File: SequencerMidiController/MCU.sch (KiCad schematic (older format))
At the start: 8 parts, among them J6 Conn_02x02_Counter_Clockwise, U33 STM32G0B1_KxTxN_LQFP32

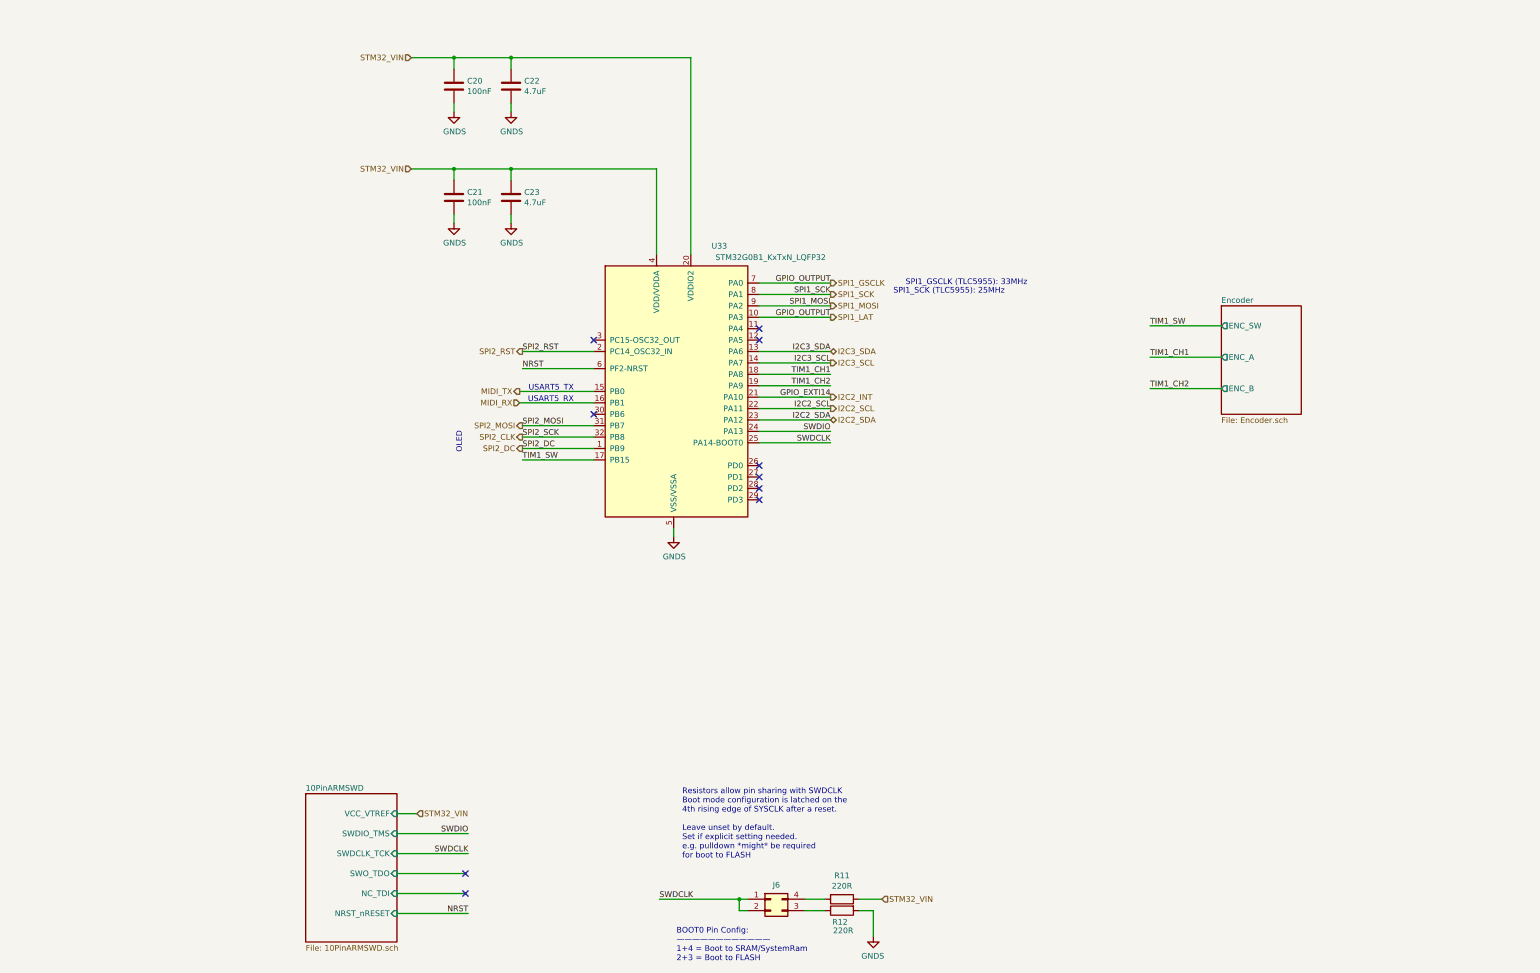
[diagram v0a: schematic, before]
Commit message: RevA Layout draft completed
- Needs tidy up
- Add test points
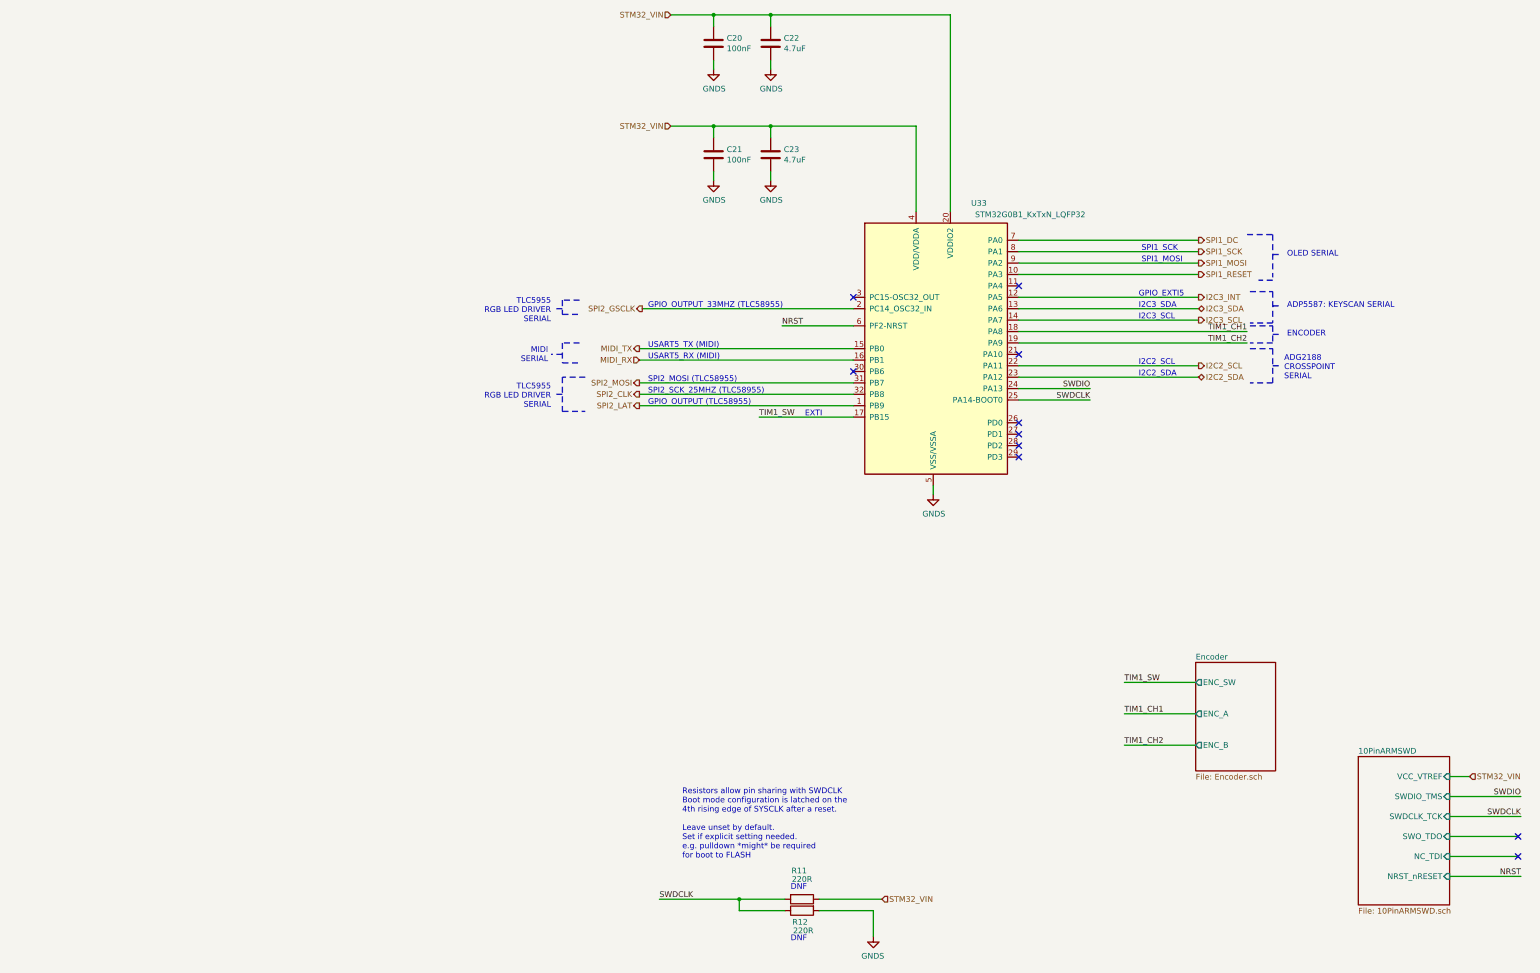
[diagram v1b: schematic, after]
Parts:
- removed J6: Conn_02x02_Counter_Clockwise, Connector_PinHeader_2.54mm:PinHeader_2x02_P2.54mm_Vertical, symbol Connector_Generic:Conn_02x02_Counter_Clockwise
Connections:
- net SWDCLK: now also R11.2, R12.1
- net I2C3_INT: now reaches U33.12 (PA5)
- net I2C2_INT: no longer names the net of U33.21 (PA10)
- net SPI1_GSCLK renamed SPI1_DC
- net SPI1_DC: no longer U33.10 (PA3)
- net SPI2_DC renamed SPI2_LAT
- net SPI2_RST renamed SPI2_GSCLK
- new net SPI1_RESET: U33.10 (PA3)
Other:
- note added: "ADG2188\nCROSSPOINT\nSERIAL"
- note added: "ADP5587: KEYSCAN SERIAL"
- note added: "DNF"
- note added: "ENCODER"
- note added: "EXTI"
- note added: "GPIO_EXTI5"
- note added: "GPIO_OUTPUT (TLC58955)"
- note added: "GPIO_OUTPUT_33MHZ (TLC58955)"
- note added: "I2C2_SCL"
- note added: "I2C2_SDA"
- note added: "I2C3_SCL"
- note added: "I2C3_SDA"
- note added: "MIDI\nSERIAL"
- note added: "OLED SERIAL"
- note added: "SPI1_MOSI"
- note added: "SPI1_SCK"
- note added: "SPI2_MOSI (TLC58955)"
- note added: "SPI2_SCK_25MHZ (TLC58955)"
- note added: "TLC5955\nRGB LED DRIVER\nSERIAL"
- note added: "USART5_RX (MIDI)"
- note added: "USART5_TX (MIDI)"
- note removed: "BOOT0 Pin Config:\n————————————\n1+4 = Boot to SRAM/SystemRam\n2+3 = Boot to FLASH"
- note removed: "OLED"
- note removed: "SPI1_GSCLK (TLC5955): 33MHz"
- note removed: "SPI1_SCK (TLC5955): 25MHz"
- note removed: "USART5_RX"
- note removed: "USART5_TX"
- moved on the sheet: C20, C21, C22, C23, R11, R12, U33

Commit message: Completed RevA layout
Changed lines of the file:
@@
 	10475 5700 10475 5625
 $Sheet
-S 14200 8000 800  1300
+S 4950 6425 800  1300
 U 63BA09FD
 F0 "10PinARMSWD" 50
 F1 "10PinARMSWD.sch" 50
-F2 "VCC_VTREF" I R 15000 8175 50
-F3 "SWDIO_TMS" I R 15000 8350 50
-F4 "SWDCLK_TCK" I R 15000 8525 50
-F5 "SWO_TDO" I R 15000 8700 50
-F6 "NC_TDI" I R 15000 8875 50
-F7 "NRST_nRESET" I R 15000 9050 50
+F2 "VCC_VTREF" I R 5750 6600 50
+F3 "SWDIO_TMS" I R 5750 6775 50
+F4 "SWDCLK_TCK" I R 5750 6950 50
+F5 "SWO_TDO" I R 5750 7125 50
+F6 "NC_TDI" I R 5750 7300 50
+F7 "NRST_nRESET" I R 5750 7475 50
 $EndSheet
 Wire Wire Line
-	15000 8175 15175 8175
-Text HLabel 15175 8175 2    50   Input ~ 0
+	5750 6600 5925 6600
+Text HLabel 5925 6600 2    50   Input ~ 0
 STM32_VIN
 Wire Wire Line
-	15000 8875 15600 8875
-NoConn ~ 15600 8875
-Wire Wire Line
-	15000 8700 15600 8700
-NoConn ~ 15600 8700
-Wire Wire Line
-	15000 9050 15625 9050
-Text Label 15625 9050 2    50   ~ 0
+	5750 7300 6350 7300
+NoConn ~ 6350 7300
+Wire Wire Line
+	5750 7125 6350 7125
+NoConn ~ 6350 7125
+Wire Wire Line
+	5750 7475 6375 7475
+Text Label 6375 7475 2    50   ~ 0
 NRST
 Wire Wire Line
@@
 NRST
 Wire Wire Line
-	15000 8525 15625 8525
-Wire Wire Line
-	15000 8350 15625 8350
-Text Label 15625 8350 2    50   ~ 0
+	5750 6950 6375 6950
+Wire Wire Line
+	5750 6775 6375 6775
+Text Label 6375 6775 2    50   ~ 0
 SWDIO
-Text Label 15625 8525 2    50   ~ 0
+Text Label 6375 6950 2    50   ~ 0
 SWDCLK
 Wire Wire Line
@@
 OLED SERIAL
 $Sheet
-S 12775 7175 700  950
+S 3000 6625 700  950
 U 68575873
 F0 "Encoder" 50
 F1 "Encoder.sch" 50
-F2 "ENC_SW" O L 12775 7350 50
-F3 "ENC_A" O L 12775 7625 50
-F4 "ENC_B" O L 12775 7900 50
+F2 "ENC_SW" O L 3000 6800 50
+F3 "ENC_A" O L 3000 7075 50
+F4 "ENC_B" O L 3000 7350 50
 $EndSheet
 Wire Wire Line
@@
 TIM1_SW
 Wire Wire Line
-	12775 7625 12150 7625
-Wire Wire Line
-	12775 7900 12150 7900
-Text Label 12150 7900 0    50   ~ 0
+	3000 7075 2375 7075
+Wire Wire Line
+	3000 7350 2375 7350
+Text Label 2375 7350 0    50   ~ 0
 TIM1_CH2
-Text Label 12150 7625 0    50   ~ 0
+Text Label 2375 7075 0    50   ~ 0
 TIM1_CH1
 Wire Wire Line
-	12775 7350 12150 7350
-Text Label 12150 7350 0    50   ~ 0
+	3000 6800 2375 6800
+Text Label 2375 6800 0    50   ~ 0
 TIM1_SW
 NoConn ~ 11225 3875

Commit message: updated for kicad 6
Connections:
- net SPI2_GSCLK: now also U33.30 (PB6); no longer U33.2 (PC14_OSC32_IN)
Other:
- note added: "GPIO_OUTPUT (TLC5955)"
- note added: "GPIO_OUTPUT_33MHZ (TLC5955)"
- note added: "SPI2_MOSI (TLC5955)"
- note added: "SPI2_SCK_25MHZ (TLC5955)"
- note removed: "GPIO_OUTPUT (TLC58955)"
- note removed: "GPIO_OUTPUT_33MHZ (TLC58955)"
- note removed: "SPI2_MOSI (TLC58955)"
- note removed: "SPI2_SCK_25MHZ (TLC58955)"
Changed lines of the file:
@@
 Comment4 ""
 $EndDescr
-$Comp
-L STM32G0B1:STM32G0B1_KxTxN_LQFP32 U33
-U 1 1 60C6B6AE
-P 10475 4425
-F 0 "U33" H 10875 5700 50  0000 C CNN
-F 1 "STM32G0B1_KxTxN_LQFP32" H 11325 5600 50  0000 C CNN
-F 2 "Package_QFP:LQFP-32_7x7mm_P0.8mm" H 10325 4775 50  0001 C CNN
-F 3 "https://www.st.com/resource/en/datasheet/stm32g0b1ke.pdf" H 10325 4775 50  0001 C CNN
-F 4 "~" H 10475 4425 50  0001 C CNN "LcscNo"
-F 5 "~" H 10475 4425 50  0001 C CNN "Type"
-	1    10475 4425
-	1    0    0    -1
-$EndComp
 Wire Wire Line
 	10325 3225 10325 2475
@@
 	9775 4925 7900 4925
 Wire Wire Line
-	9775 4075 7925 4075
+	9775 4625 7900 4625
 Text HLabel 7900 4925 0    50   Output ~ 0
 SPI2_LAT
-Text HLabel 7925 4075 0    50   Output ~ 0
+Text HLabel 7900 4625 0    50   Output ~ 0
 SPI2_GSCLK
 Wire Wire Line
@@
 NoConn ~ 11225 3875
 NoConn ~ 11225 4475
-NoConn ~ 9775 4625
 NoConn ~ 9775 3975
 Text Notes 9225 9625 0    50   ~ 0
@@
 	13450 3600 13525 3600
 Text Notes 7975 4925 0    50   ~ 0
-GPIO_OUTPUT (TLC58955)
+GPIO_OUTPUT (TLC5955)
 Text Notes 7975 4825 0    50   ~ 0
-SPI2_SCK_25MHZ (TLC58955)
+SPI2_SCK_25MHZ (TLC5955)
 Text Notes 7975 4725 0    50   ~ 0
-SPI2_MOSI (TLC58955)
-Text Notes 7975 4075 0    50   ~ 0
-GPIO_OUTPUT_33MHZ (TLC58955)
+SPI2_MOSI (TLC5955)
+Text Notes 7975 4625 0    50   ~ 0
+GPIO_OUTPUT_33MHZ (TLC5955)
 Text Notes 12275 4075 0    50   ~ 0
 I2C3_SDA
@@
 Wire Notes Line
 	13450 4725 13250 4725
-Text Notes 7125 4200 2    50   ~ 0
+Wire Notes Line
+	7425 4575 7225 4575
+Wire Notes Line
+	7225 4575 7225 4975
+Wire Notes Line
+	7225 4975 7425 4975
+Text Notes 7125 4900 2    50   ~ 0
 TLC5955\nRGB LED DRIVER\nSERIAL
 Wire Notes Line
-	7425 4675 7225 4675
-Wire Notes Line
-	7225 4075 7150 4075
-Wire Notes Line
-	7225 4675 7225 4975
-Wire Notes Line
-	7225 4975 7425 4975
-Text Notes 7125 4950 2    50   ~ 0
-TLC5955\nRGB LED DRIVER\nSERIAL
-Wire Notes Line
-	7225 4825 7150 4825
-Wire Notes Line
-	7375 4000 7225 4000
-Wire Notes Line
-	7225 4000 7225 4125
-Wire Notes Line
-	7225 4125 7375 4125
+	7225 4775 7150 4775
 Text Notes 7100 4550 2    50   ~ 0
 MIDI\nSERIAL
@@
 NoConn ~ 11225 5275
 NoConn ~ 11225 5375
+$Comp
+L STM32G0B1:STM32G0B1_KxTxN_LQFP32 U33
+U 1 1 60C6B6AE
+P 10475 4425
+F 0 "U33" H 10875 5700 50  0000 C CNN
+F 1 "STM32G0B1_KxTxN_LQFP32" H 11325 5600 50  0000 C CNN
+F 2 "Package_QFP:LQFP-32_7x7mm_P0.8mm" H 10325 4775 50  0001 C CNN
+F 3 "https://www.st.com/resource/en/datasheet/stm32g0b1ke.pdf" H 10325 4775 50  0001 C CNN
+F 4 "~" H 10475 4425 50  0001 C CNN "LcscNo"
+F 5 "~" H 10475 4425 50  0001 C CNN "Type"
+	1    10475 4425
+	1    0    0    -1
+$EndComp
+NoConn ~ 9775 4075
 $EndSCHEMATC
